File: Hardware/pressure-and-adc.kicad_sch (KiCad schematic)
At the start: 1 part, among them U5 ADS1115IDGSR

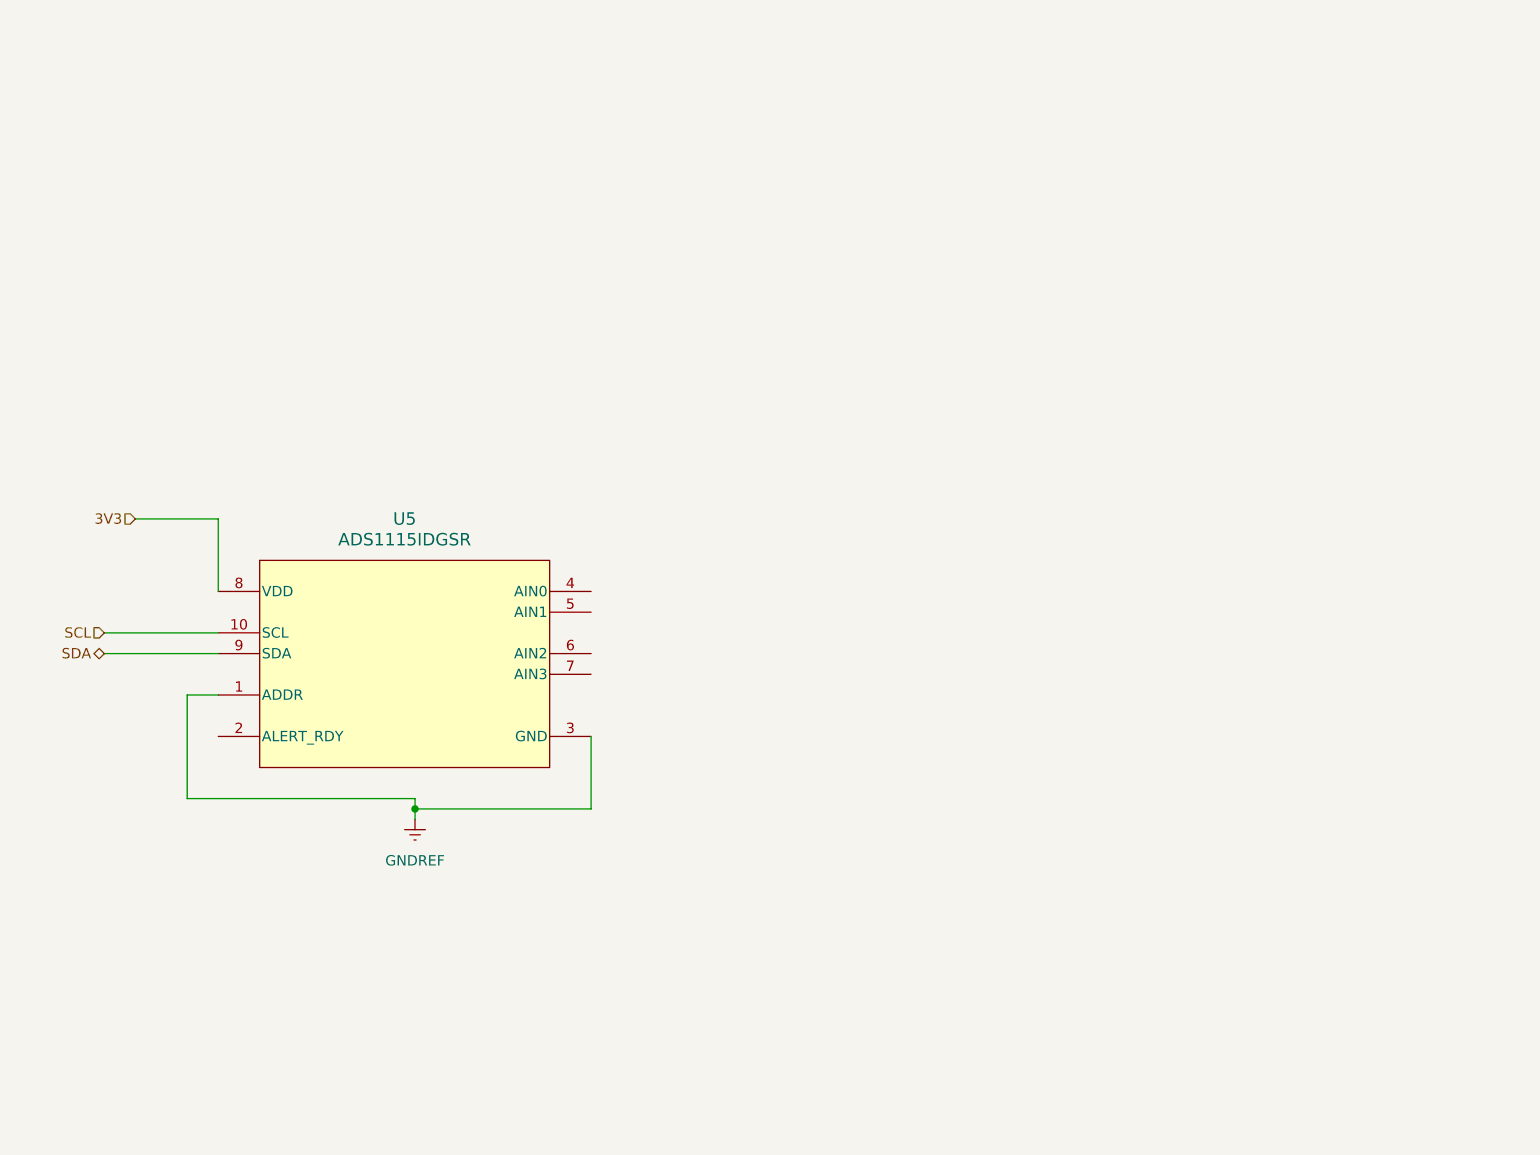
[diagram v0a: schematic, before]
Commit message: Use Peanut symbols, fix ERC errors, progress on DAC & Pressure
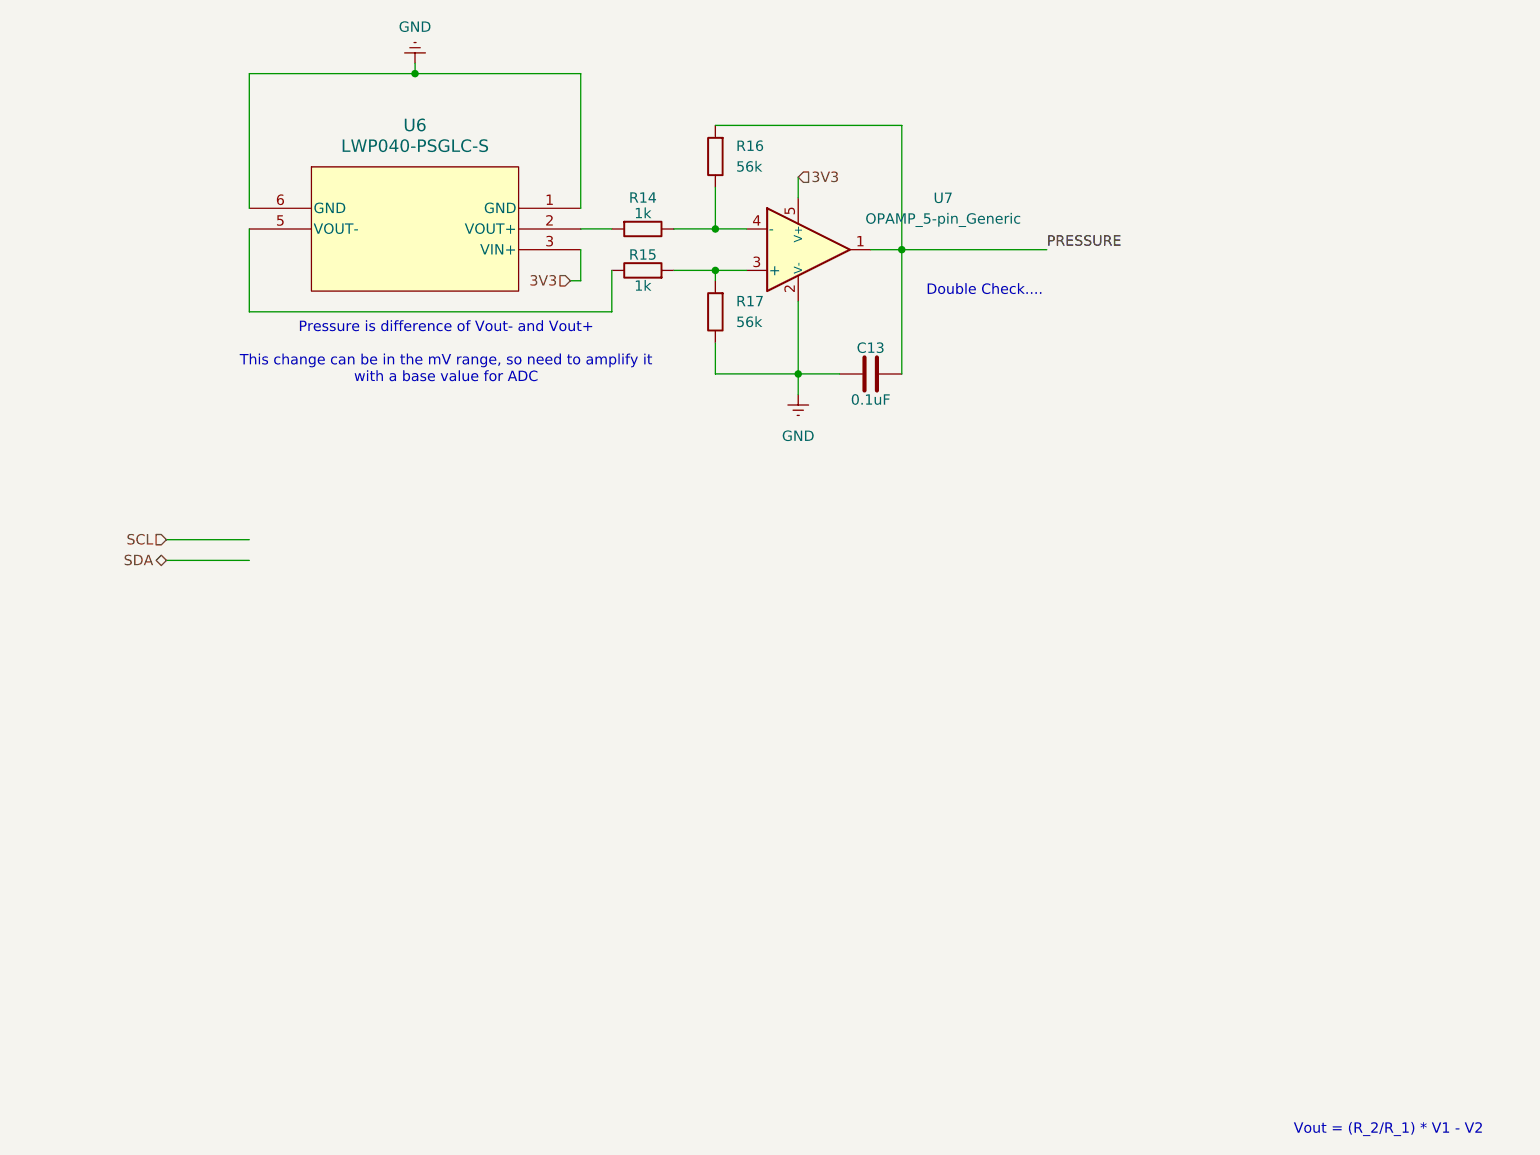
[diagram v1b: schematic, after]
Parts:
- removed U5: ADS1115IDGSR, Snapeda:DGS0010A_N, symbol Peanut:ADS1115IDGSR
- added C13: 0.1uF, Capacitor_SMD:C_0201_0603Metric, symbol Device:C
- added R14, R15: 1k, Resistor_SMD:R_0201_0603Metric, symbol Peanut:R
- added R16, R17: 56k, Resistor_SMD:R_0201_0603Metric, symbol Peanut:R
- added U6: LWP040-PSGLC-S, Peanut:SOP-4_L7.0-W7.0-P2.54-LS10.3-TL-CW_LWP040-PSGLC-S, symbol Peanut:LWP040-PSGLC-S
- added U7: OPAMP_5-pin_Generic, symbol PCM_Amplifier_Operational_AKL:OPAMP_5-pin_Generic
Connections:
- net 3V3: now also U6.3 (VIN+), U7.5 (V+)
- new net: R15.1, R17.1, U7.3 (+)
- new net: R14.2, R16.2, U7.4 (-)
- new net: R14.1, U6.2 (VOUT+)
- new net: R15.2, U6.5 (VOUT-)
- new net GND: C13.1, R17.2, U6.1 (GND), U6.6 (GND), U7.2 (V-)
- new net PRESSURE: C13.2, R16.1, U7.1
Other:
- note added: "Double Check...."
- note added: "Pressure is difference of Vout- and Vout+ This change can be in the mV range, so need to amplify it with a base value for ADC"
- note added: "Vout = (R_2/R_1) * V1 - V2"

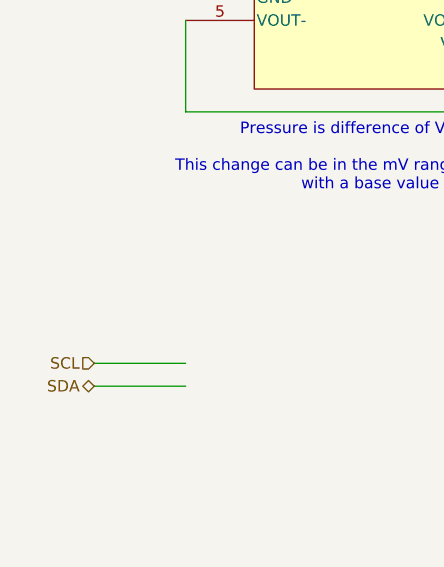
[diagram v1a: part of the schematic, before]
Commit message: Replace 1 LED with battery measurement toggle - We require an additional IO to toggle battery draining for % measurement, however we had no more ports. After a group discussion, one LED was dropped.
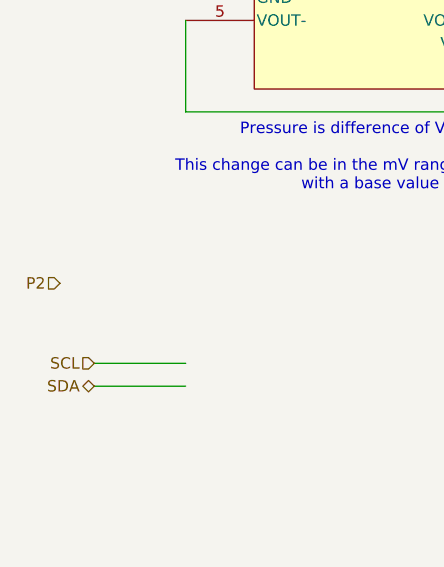
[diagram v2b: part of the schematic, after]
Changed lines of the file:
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@@
+		)
+	)
+	(hierarchical_label "P2"
+		(shape input)
+		(at 100.33 78.74 180)
+		(fields_autoplaced yes)
+		(effects
+			(font
+				(size 1.27 1.27)
+			)
+			(justify right)
 		)
 	)

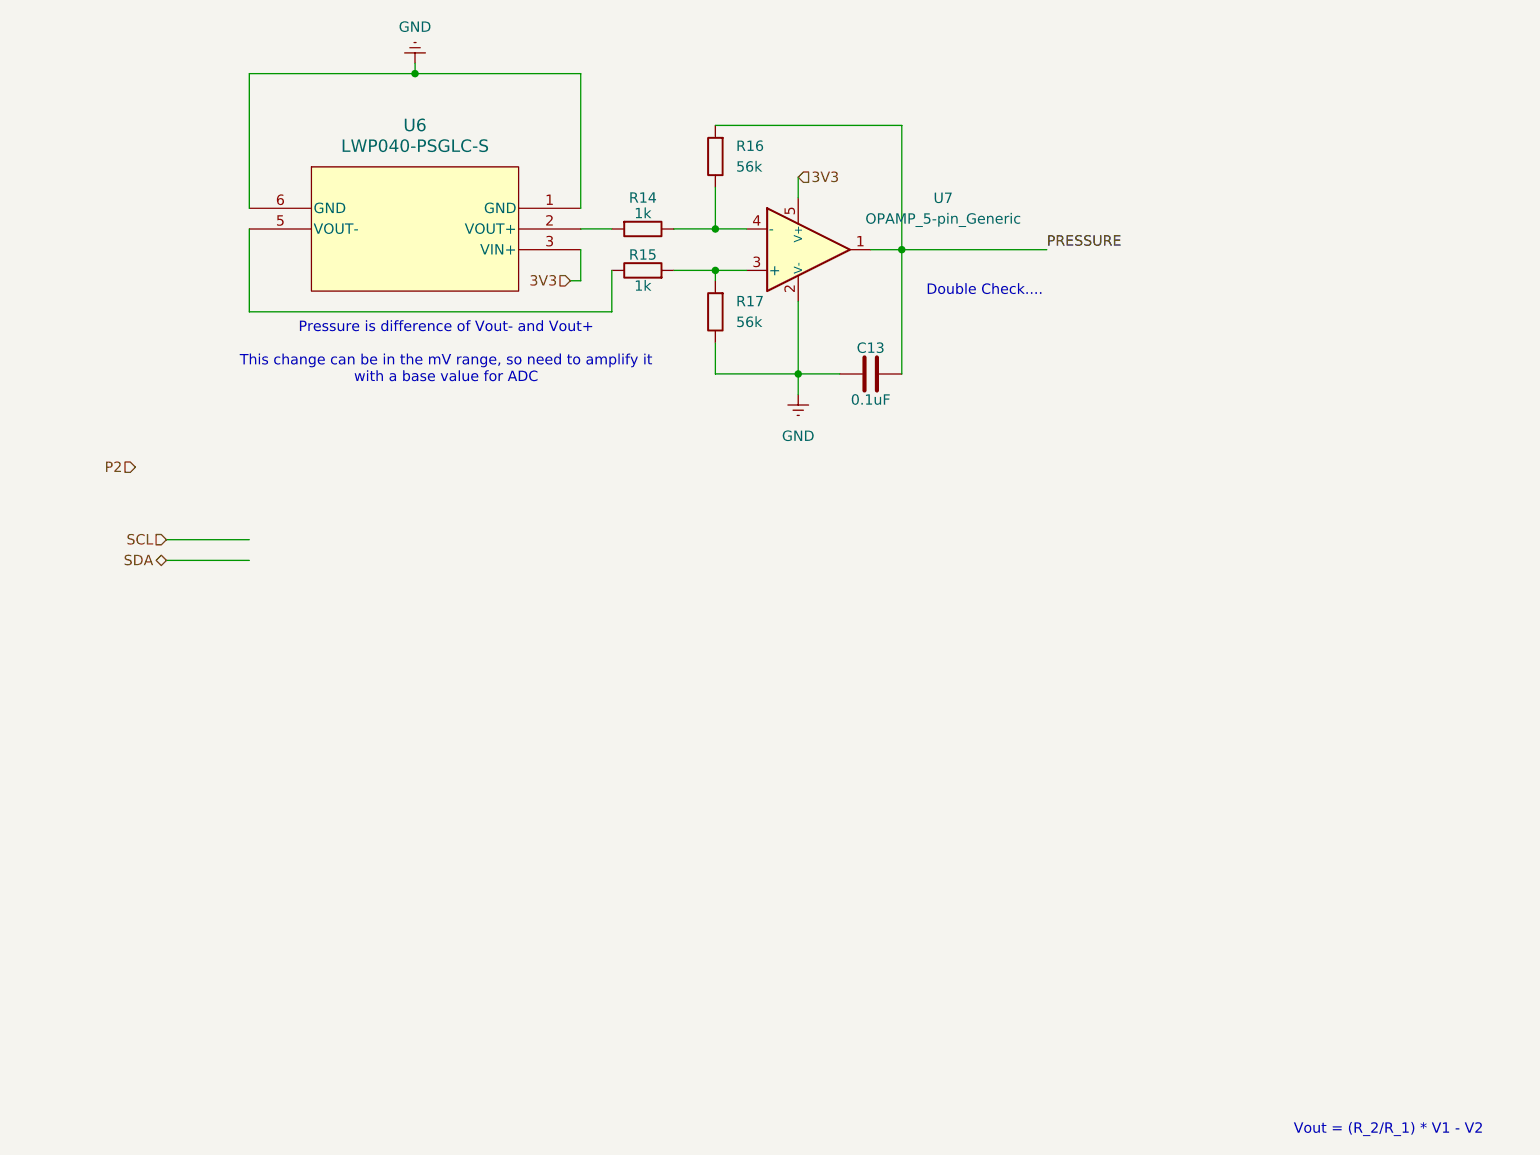
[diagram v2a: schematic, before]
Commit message: Add Battery Monitoring & Use Project Parts Library
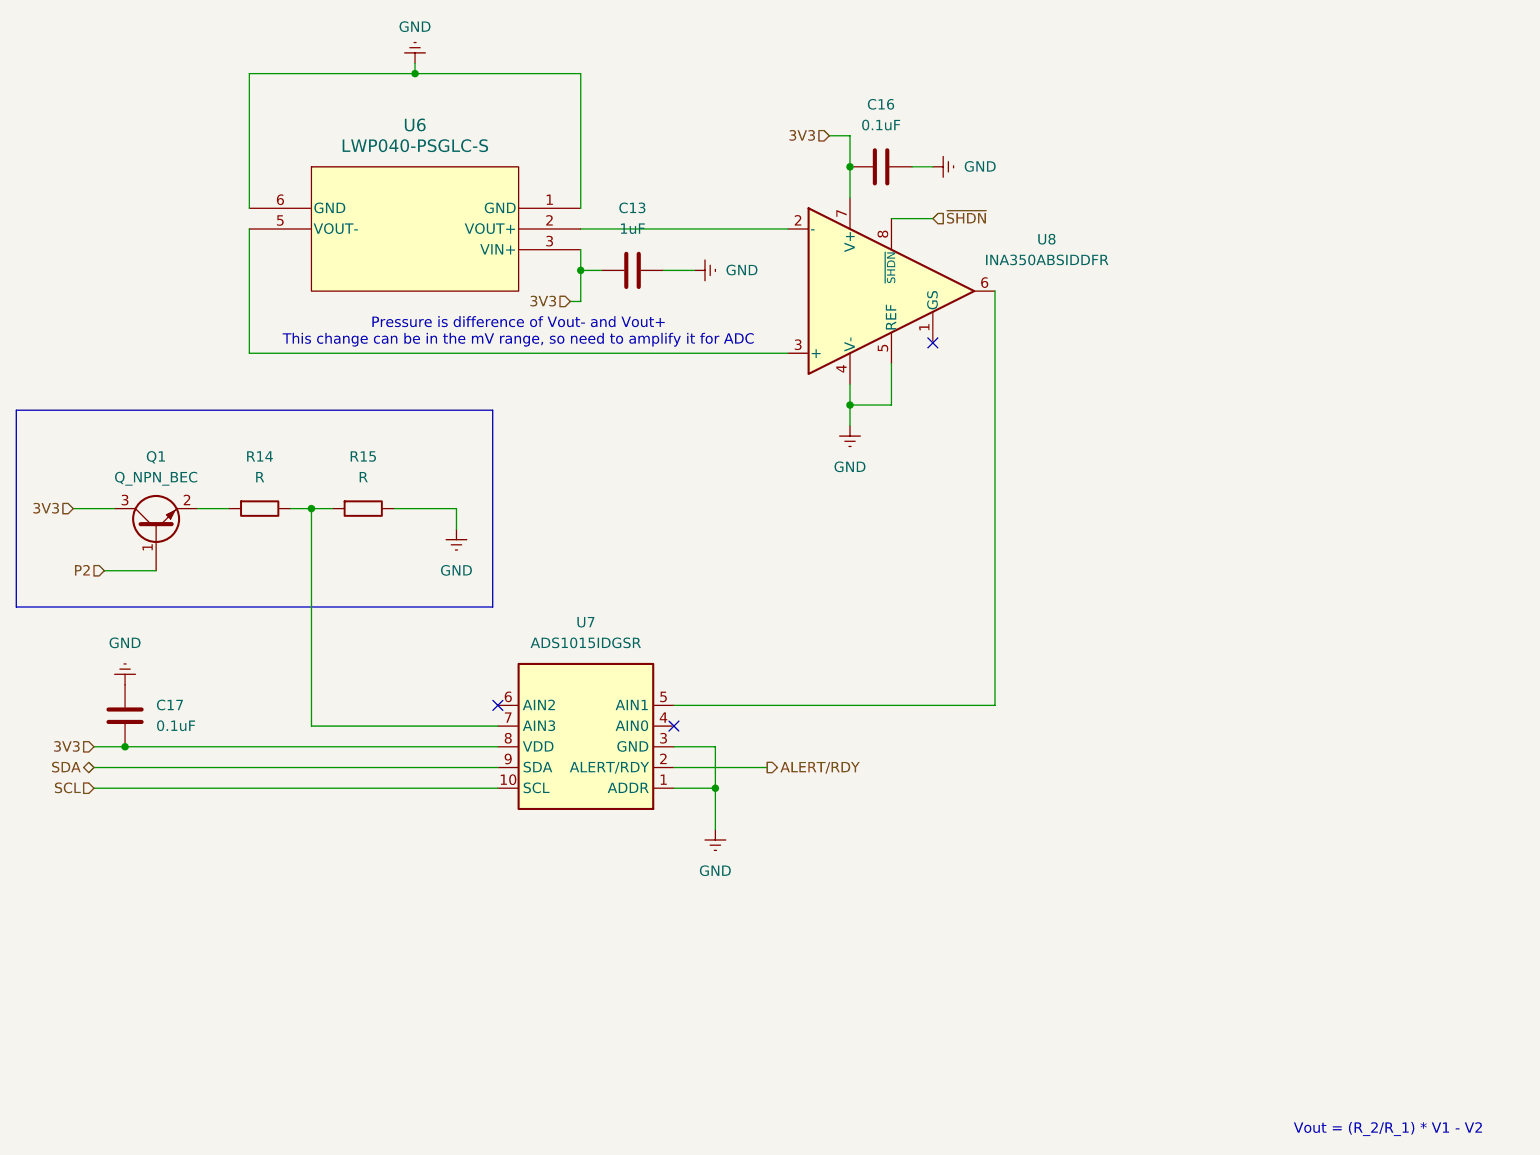
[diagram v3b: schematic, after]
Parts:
- removed R16, R17: 56k, Resistor_SMD:R_0201_0603Metric, symbol Peanut:R
- removed U7: OPAMP_5-pin_Generic, symbol PCM_Amplifier_Operational_AKL:OPAMP_5-pin_Generic
- added C16, C17: 0.1uF, symbol Device:C
- added Q1: Q_NPN_BEC, symbol Device:Q_NPN_BEC
- added U7: ADS1015IDGSR, Package_SO:VSSOP-10_3x3mm_P0.5mm, symbol Peanut:ADS1015IDGS
- added U8: INA350ABSIDDFR, Package_TO_SOT_SMD:TSOT-23-8, symbol Peanut:INA350ABSIDDFR
- C13: value 0.1uF -> 1uF; footprint Capacitor_SMD:C_0201_0603Metric -> (none)
- R14, R15: value 1k -> R
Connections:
- net PRESSURE is gone; now on net GND: C13.2
- net 3V3: now also C13.1, C16.1, C17.1, Q1.3 (C), U7.8 (VDD), U8.7 (V+)
- net GND: now also R15.2, C16.2, C17.2, U7.1 (ADDR), U7.3 (GND), U8.4 (V-), U8.5 (REF); no longer C13.1
- net P2: now also Q1.1 (B)
- net SCL: now also U7.10 (SCL)
- net SDA: now also U7.9 (SDA)
- net at R15.1: now also R14.2, U7.7 (AIN3)
- net at U6.2 (VOUT+): now also U8.2 (-); no longer R14.1
- net at U6.5 (VOUT-): now also U8.3 (+); no longer R15.2
- new net: U7.5 (AIN1), U8.6
- new net: Q1.2 (E), R14.1
- new net ALERT/RDY: U7.2 (ALERT/RDY)
- new net ~{SHDN}: U8.8 (~{SHDN})
- no-connect marks 0 -> 3
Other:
- note added: "Pressure is difference of Vout- and Vout+ This change can be in the mV range, so need to amplify it for ADC"
- note removed: "Double Check...."
- note removed: "Pressure is difference of Vout- and Vout+ This change can be in the mV range, so need to amplify it with a base value for ADC"

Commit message: Fully wired board!
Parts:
- C13, C16, C17: footprint (none) -> Resistor_SMD:R_01005_0402Metric; symbol Device:C -> Peanut:C
- Q1: footprint (none) -> Package_TO_SOT_SMD:SOT-23-3; symbol Device:Q_NPN_BEC -> Peanut:Transistor_BEC
- R14, R15: footprint Resistor_SMD:R_0201_0603Metric -> Resistor_SMD:R_0402_1005Metric
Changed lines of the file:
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@@
 			)
 		)
-		(property "Footprint" "Resistor_SMD:R_0201_0603Metric"
+		(property "Footprint" "Resistor_SMD:R_0402_1005Metric"
 			(at 116.459 88.138 0)
 			(effects
@@
 	)
 	(symbol
-		(lib_id "Device:C")
+		(lib_id "Peanut:C")
 		(at 99.06 109.22 180)
 		(unit 1)
@@
 			)
 		)
-		(property "Footprint" ""
+		(property "Footprint" "Resistor_SMD:R_01005_0402Metric"
 			(at 98.0948 105.41 0)
 			(effects
@@
 	)
 	(symbol
-		(lib_id "Device:Q_NPN_BEC")
+		(lib_id "Peanut:Transistor_BEC")
 		(at 102.87 86.36 90)
 		(unit 1)
@@
 			)
 		)
-		(property "Footprint" ""
+		(property "Footprint" "Package_TO_SOT_SMD:SOT-23-3"
 			(at 100.33 81.28 0)
 			(effects
@@
 		)
 		(property "Description" "NPN transistor, base/emitter/collector"
-			(at 102.87 86.36 0)
+			(at 112.522 85.598 0)
 			(effects
 				(font
@@
 	)
 	(symbol
-		(lib_id "Device:C")
+		(lib_id "Peanut:C")
 		(at 191.77 41.91 90)
 		(unit 1)
@@
 			)
 		)
-		(property "Footprint" ""
+		(property "Footprint" "Resistor_SMD:R_01005_0402Metric"
 			(at 195.58 40.9448 0)
 			(effects
@@
 			)
 		)
-		(property "Footprint" "Resistor_SMD:R_0201_0603Metric"
+		(property "Footprint" "Resistor_SMD:R_0402_1005Metric"
 			(at 129.159 88.138 0)
 			(effects
@@
 	)
 	(symbol
-		(lib_id "Device:C")
+		(lib_id "Peanut:C")
 		(at 161.29 54.61 90)
 		(unit 1)
@@
 			)
 		)
-		(property "Footprint" ""
+		(property "Footprint" "Resistor_SMD:R_01005_0402Metric"
 			(at 165.1 53.6448 0)
 			(effects
